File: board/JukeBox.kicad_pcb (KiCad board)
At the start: 2 copper layers, 78.5 x 80 mm, 56 parts, among them J1 USB_C_Receptacle_USB2.0, J2 Conn_01x02, J3 Conn_01x04, J4 Conn_01x03, SW1 SW_SPST, SW10 SW_SPST, SW11 SW_SPST, SW12 SW_SPST, SW2 SW_SPST, SW3 SW_SPST, SW4 SW_SPST, SW5 SW_SPST, SW6 SW_SPST, SW7 SW_SPST, SW8 SW_SPST, SW9 SW_SPST, U1 ATmega8U2-A, Y1 16MHz

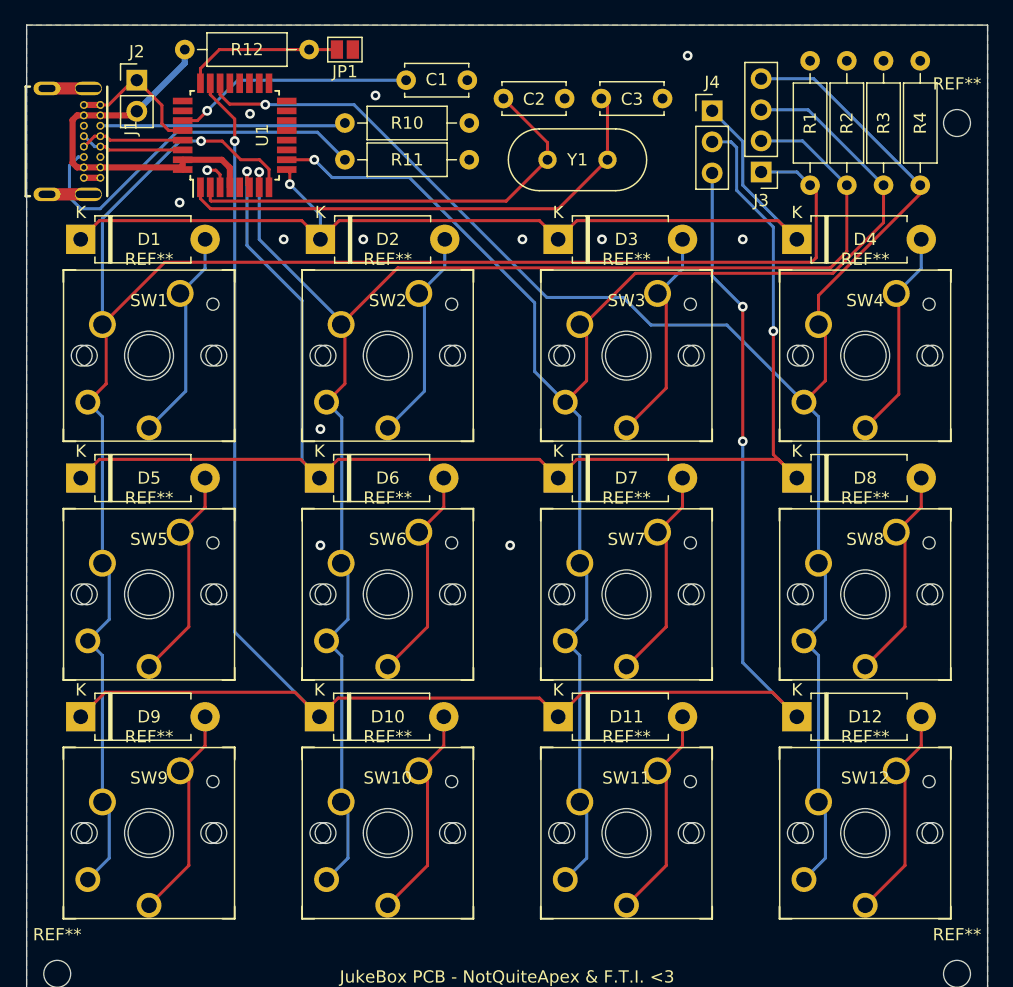
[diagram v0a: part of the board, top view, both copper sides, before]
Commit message: reroute everything again to move the mcu over
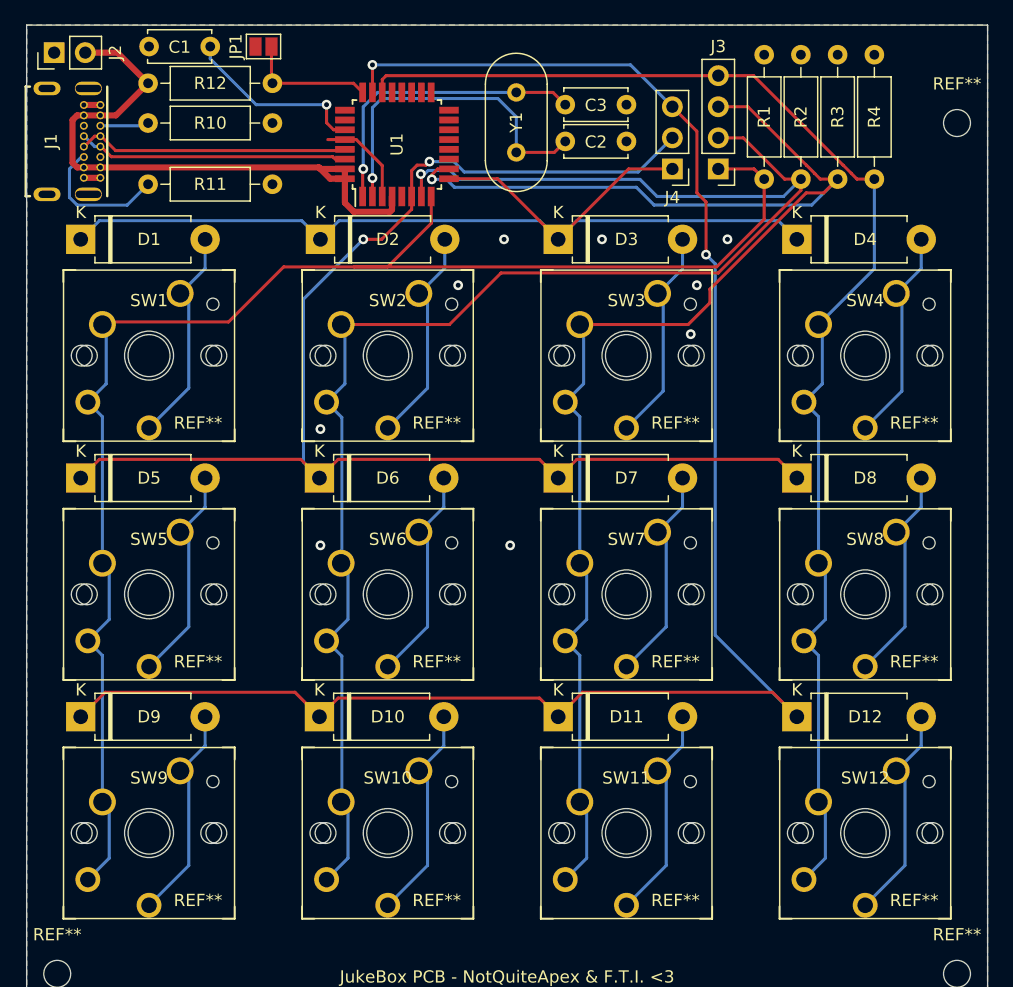
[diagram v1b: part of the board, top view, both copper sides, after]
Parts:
- moved C1 26.1 mm to (117.0, 36.8), turned to 0 degrees
- moved R11 16.2 mm to (116.9, 48.0)
- moved R10 16.1 mm to (116.9, 43.0)
- moved U1 13.3 mm to (137.2, 44.8)
- moved Y1 9.26 mm to (147.0, 40.5), turned to -90 degrees
- moved J2 7.12 mm to (109.2, 37.2), turned to 90 degrees
- moved JP1 6.65 mm to (126.3, 36.8), turned to 0 degrees
- moved C2 6.14 mm to (156.0, 44.5)
- moved J4 5.76 mm to (159.8, 46.8), turned to 180 degrees
- moved R12 4.07 mm to (127.1, 39.8)
- moved R1 3.78 mm to (167.2, 37.4)
- moved R2 3.78 mm to (170.2, 37.4)
- moved R3 3.78 mm to (173.2, 37.4)
- moved R4 3.78 mm to (176.2, 37.4)
- moved J3 3.51 mm to (163.5, 46.8)
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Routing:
- net COL_4: track 139.7 -> 107.6 mm, vias 1 -> 0
- net COL_1: track 147.2 -> 124.0 mm, vias 1 -> 0
- net ROW_3: track 165.8 -> 145.3 mm, vias 3 -> 2
- net Net-(J1-PadB5): track 30.5 -> 11.3 mm
- net +5V: track 31.5 -> 50.1 mm
- net Net-(C3-Pad2): track 41.4 -> 24.7 mm, vias 0 -> 1
- net Net-(J1-PadA5): track 20.1 -> 3.99 mm
- net /D+: track 8.56 -> 22.2 mm
- net /D-: track 8.54 -> 21.4 mm
- net COL_2: track 123.1 -> 134.7 mm
- net GND: track 22.0 -> 10.6 mm, vias 13 -> 9
- net Net-(C2-Pad2): track 36.5 -> 27.2 mm, vias 0 -> 1
- net ROW_2: track 122.4 -> 115.6 mm
- net Net-(C1-Pad2): track 19.6 -> 15.3 mm
- net ROW_1: track 82.5 -> 85.0 mm, vias 1 -> 0
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
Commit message: update models
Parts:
- renumbered REF** to _
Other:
- outline, holes or cut-outs redrawn
- board text added: "JukeBox - NotQuiteApex & F.T.I. <3"
- board text added: "https://jukebox.friendteam.biz"
- board text removed: "JukeBox PCB - NotQuiteApex & F.T.I. <3"

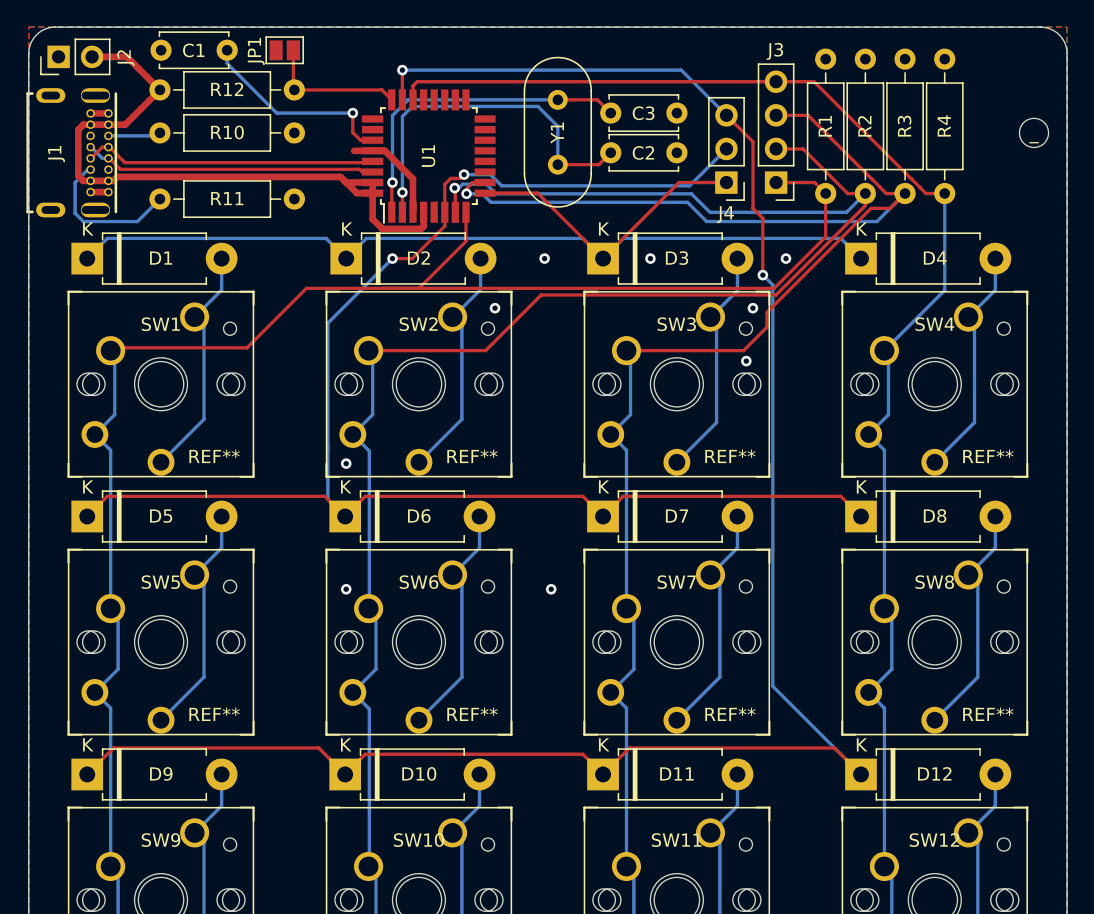
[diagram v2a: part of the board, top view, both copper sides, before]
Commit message: add footprint for screen addon, change all tht components to smt
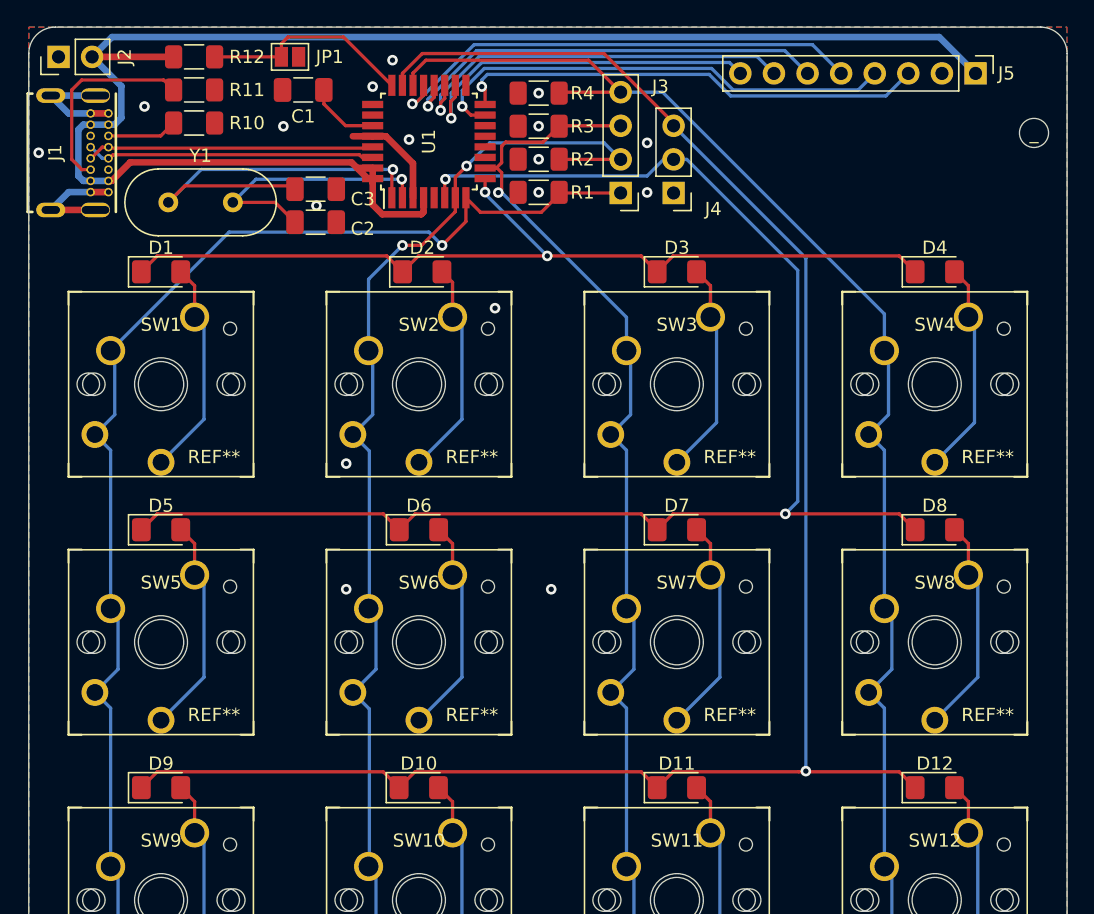
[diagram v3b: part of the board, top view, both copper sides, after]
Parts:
- added J5: Conn_01x08, Connector_PinHeader_2.54mm:PinHeader_1x08_P2.54mm_Vertical, F.Cu at (178.6, 38.5)
- C1, C2, C3: footprint Capacitor_THT:C_Disc_D5.0mm_W2.5mm_P5.00mm -> Capacitor_SMD:C_1206_3216Metric_Pad1.33x1.80mm_HandSolder
- D1, D10, D11, D12, D2, D3, D4, D5, D6, D7, D8, D9: footprint Diode_THT:D_DO-15_P10.16mm_Horizontal -> Diode_SMD:D_1206_3216Metric_Pad1.42x1.75mm_HandSolder
- R1, R10, R11, R12, R2, R3, R4: footprint Resistor_THT:R_Axial_DIN0207_L6.3mm_D2.5mm_P10.16mm_Horizontal -> Resistor_SMD:R_1206_3216Metric_Pad1.30x1.75mm_HandSolder
- Y1: footprint Crystal:Crystal_HC18-U_Vertical -> Crystal:Crystal_HC49-4H_Vertical
- moved R4 30.8 mm to (145.6, 40.0), turned to 0 degrees
- moved Y1 30.5 mm to (117.5, 48.2), turned to 0 degrees
- moved R3 28.2 mm to (145.6, 42.5), turned to 0 degrees
- moved C3 27.9 mm to (128.7, 47.2)
- moved C2 27.8 mm to (128.7, 49.8)
- moved R2 25.8 mm to (145.6, 45.0), turned to 0 degrees
- moved R1 23.9 mm to (145.6, 47.5), turned to 0 degrees
- moved J3 11.8 mm to (151.8, 47.5)
- moved C1 11.2 mm to (127.8, 39.8)
- moved R11 8.64 mm to (119.5, 39.8)
- moved R12 7.98 mm to (119.5, 37.2)
- moved D2 5.84 mm to (136.8, 53.5)
- moved D11 5.67 mm to (156.0, 92.5)
- moved D12 5.67 mm to (175.5, 92.5)
- moved D3 5.67 mm to (156.0, 53.5)
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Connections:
- U1 pad 15: unconnected-(U1-Pad15) -> CLK
- U1 pad 16: unconnected-(U1-Pad16) -> DIN
- U1 pad 18: unconnected-(U1-Pad18) -> BL
- U1 pad 19: unconnected-(U1-Pad19) -> RST
- U1 pad 20: unconnected-(U1-Pad20) -> DC
- U1 pad 21: unconnected-(U1-Pad21) -> CS
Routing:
- net +5V: track 50.4 -> 120.1 mm
- net COL_2: track 134.7 -> 84.4 mm, vias 1 -> 2
- net COL_3: track 124.7 -> 80.4 mm
- net CS: track 0.00 -> 37.0 mm, vias 0 -> 1
- net CLK: track 0.00 -> 36.3 mm, vias 0 -> 1
- net DIN: track 0.00 -> 35.8 mm, vias 0 -> 1
- net DC: track 0.00 -> 33.2 mm, vias 0 -> 1
- net RST: track 0.00 -> 30.1 mm, vias 0 -> 1
- net COL_1: track 124.0 -> 95.4 mm, vias 0 -> 1
- net BL: track 0.00 -> 27.7 mm, vias 0 -> 1
- net ROW_1: track 85.0 -> 69.3 mm, vias 0 -> 2
- net GND: track 10.6 -> 24.6 mm, vias 9 -> 17
- net Net-(C1-Pad2): track 15.3 -> 5.43 mm, vias 1 -> 0
- net Net-(C2-Pad2): track 27.2 -> 20.2 mm
- net ROW_3: track 145.3 -> 138.8 mm, vias 2 -> 1
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
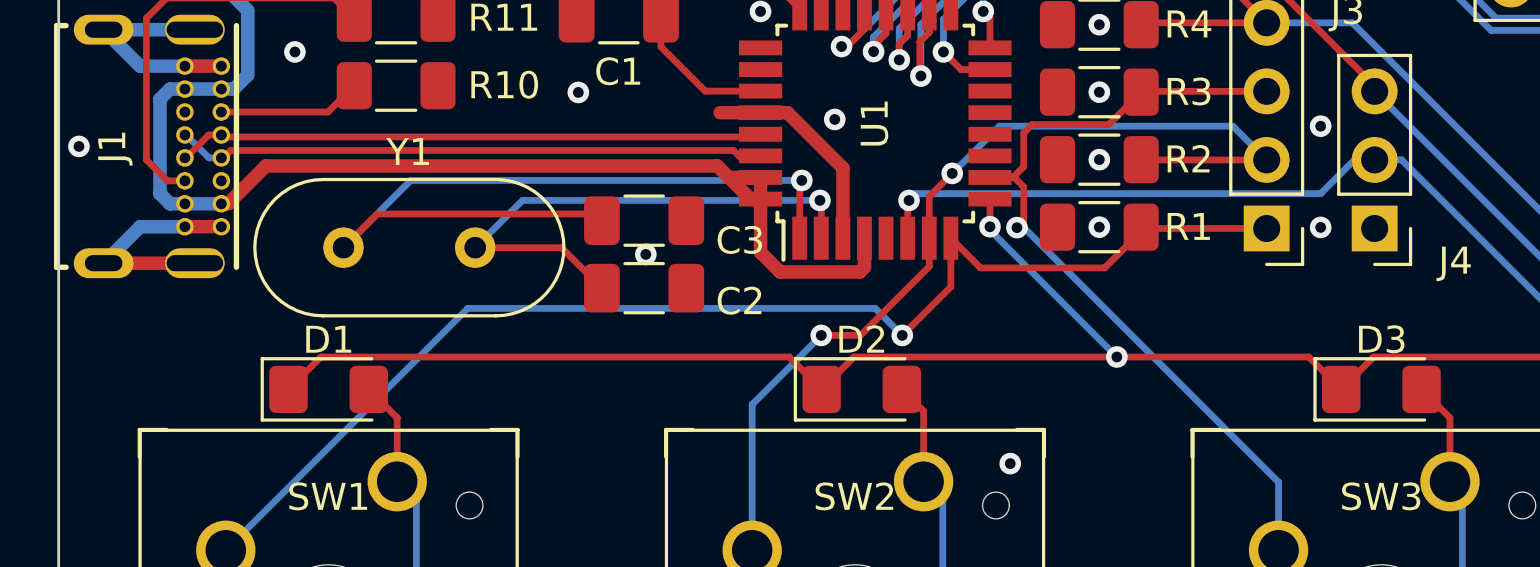
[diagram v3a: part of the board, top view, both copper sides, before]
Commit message: ran a drc, fix some errors
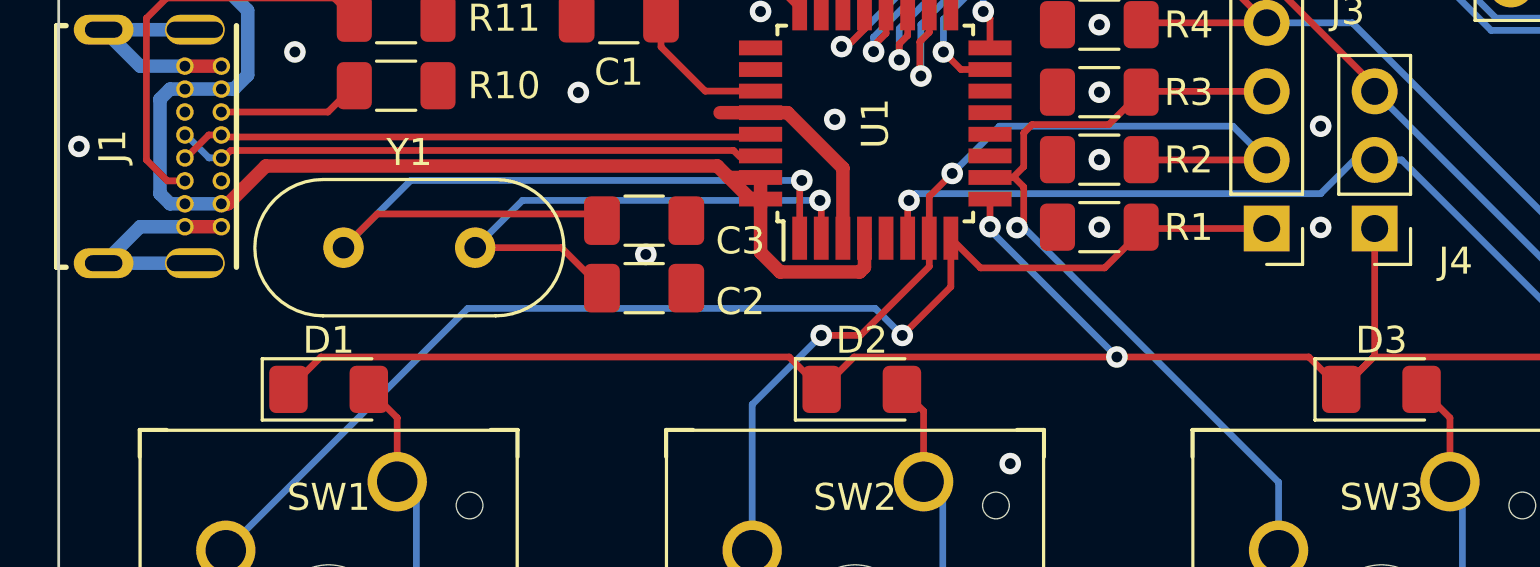
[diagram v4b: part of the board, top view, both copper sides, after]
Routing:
- net ROW_1: track 69.3 -> 75.8 mm
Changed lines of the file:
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@@
   (segment (start 136.05 45.3) (end 136.05 47.9) (width 0.5) (layer "F.Cu") (net 1))
   (segment (start 133 43.25) (end 131.5 43.25) (width 0.5) (layer "F.Cu") (net 1))
-  (segment (start 108.665 48.825) (end 112.045 48.825) (width 0.5) (layer "F.Cu") (net 1))
   (segment (start 111.675 41.525) (end 113.025 41.525) (width 0.5) (layer "F.Cu") (net 1))
   (segment (start 133 43.25) (end 134 43.25) (width 0.5) (layer "F.Cu") (net 1))
@@
   (segment (start 110.015 47.475) (end 108.665 48.825) (width 0.5) (layer "B.Cu") (net 1))
   (segment (start 111.675 47.475) (end 110.015 47.475) (width 0.5) (layer "B.Cu") (net 1))
+  (segment (start 108.665 48.825) (end 112.045 48.825) (width 0.5) (layer "B.Cu") (net 1))
   (segment (start 112.045 40.175) (end 108.665 40.175) (width 0.5) (layer "B.Cu") (net 1))
   (segment (start 111.675 41.525) (end 110.015 41.525) (width 0.5) (layer "B.Cu") (net 1))
@@
   (segment (start 134.528649 45.759985) (end 120.040015 45.759985) (width 0.25) (layer "B.Cu") (net 4))
   (segment (start 153.3125 52.3) (end 154.5125 53.5) (width 0.25) (layer "F.Cu") (net 5))
+  (segment (start 155.75 47.54) (end 155.75 52.2625) (width 0.25) (layer "F.Cu") (net 5))
   (segment (start 136.4625 52.3) (end 146.2 52.3) (width 0.25) (layer "F.Cu") (net 5))
   (segment (start 155.7125 52.3) (end 154.5125 53.5) (width 0.25) (layer "F.Cu") (net 5))
@@
   (segment (start 141.5 46.45) (end 141.5 47.4755) (width 0.25) (layer "F.Cu") (net 5))
   (segment (start 134.0625 52.3) (end 135.2625 53.5) (width 0.25) (layer "F.Cu") (net 5))
+  (segment (start 155.75 52.2625) (end 154.5125 53.5) (width 0.25) (layer "F.Cu") (net 5))
   (segment (start 115.5125 53.5) (end 116.7125 52.3) (width 0.25) (layer "F.Cu") (net 5))
   (segment (start 155.7125 52.3) (end 172.8125 52.3) (width 0.25) (layer "F.Cu") (net 5))
@@
   (segment (start 142.75 45.25) (end 142.75 44) (width 0.25) (layer "F.Cu") (net 30))
   (segment (start 151.75 42.46) (end 147.13 42.46) (width 0.25) (layer "F.Cu") (net 30))
-  (segment (start 142.75 46) (end 142.75 47.257102) (width 0.25) (layer "F.Cu") (net 30))
+  (segment (start 142.75 46) (end 142.4 45.65) (width 0.25) (layer "F.Cu") (net 30))
   (segment (start 142.75 44) (end 143.06 43.69) (width 0.25) (layer "F.Cu") (net 30))
   (segment (start 141.5 45.65) (end 142.35 45.65) (width 0.25) (layer "F.Cu") (net 30))
-  (segment (start 141.5 45.65) (end 142.4 45.65) (width 0.25) (layer "F.Cu") (net 30))
+  (segment (start 142.75 47.257102) (end 142.75 46) (width 0.25) (layer "F.Cu") (net 30))
   (segment (start 147.13 42.46) (end 147.1 42.49) (width 0.25) (layer "F.Cu") (net 30))
   (segment (start 145.9 43.69) (end 147.1 42.49) (width 0.25) (layer "F.Cu") (net 30))
   (segment (start 143.06 43.69) (end 145.9 43.69) (width 0.25) (layer "F.Cu") (net 30))
-  (segment (start 142.4 45.65) (end 142.75 46) (width 0.25) (layer "F.Cu") (net 30))
-  (segment (start 142.75 47.257102) (end 142.498969 47.508133) (width 0.25) (layer "F.Cu") (net 30))
+  (segment (start 142.498969 47.508133) (end 142.75 47.257102) (width 0.25) (layer "F.Cu") (net 30))
+  (segment (start 142.4 45.65) (end 141.5 45.65) (width 0.25) (layer "F.Cu") (net 30))
   (via (at 142.498969 47.508133) (size 0.8) (drill 0.4) (layers "F.Cu" "B.Cu") (net 30))
   (segment (start 152.5 64.3) (end 152.5 59.77) (width 0.25) (layer "B.Cu") (net 30))
   (segment (start 152.75 79.52) (end 152.19 78.96) (width 0.25) (layer "B.Cu") (net 30))
   (segment (start 152.19 56.94) (end 152.19 59.46) (width 0.25) (layer "B.Cu") (net 30))
+  (segment (start 142.758133 47.508133) (end 152.19 56.94) (width 0.25) (layer "B.Cu") (net 30))
   (segment (start 152.75 103.05) (end 152.75 99.02) (width 0.25) (layer "B.Cu") (net 30))
   (segment (start 152.5 59.77) (end 152.19 59.46) (width 0.25) (layer "B.Cu") (net 30))
@@
   (segment (start 151 65.8) (end 152.19 66.99) (width 0.25) (layer "B.Cu") (net 30))
   (segment (start 151 65.8) (end 152.5 64.3) (width 0.25) (layer "B.Cu") (net 30))
+  (segment (start 142.498969 47.508133) (end 142.758133 47.508133) (width 0.25) (layer "B.Cu") (net 30))
   (segment (start 152.75 99.02) (end 152.19 98.46) (width 0.25) (layer "B.Cu") (net 30))
   (segment (start 151 85.3) (end 152.19 86.49) (width 0.25) (layer "B.Cu") (net 30))
-  (segment (start 142.498969 47.508133) (end 142.758133 47.508133) (width 0.25) (layer "B.Cu") (net 30))
   (segment (start 151 85.3) (end 152.75 83.55) (width 0.25) (layer "B.Cu") (net 30))
   (segment (start 152.75 83.55) (end 152.75 79.52) (width 0.25) (layer "B.Cu") (net 30))
   (segment (start 152.19 66.99) (end 152.19 78.96) (width 0.25) (layer "B.Cu") (net 30))
-  (segment (start 142.758133 47.508133) (end 152.19 56.94) (width 0.25) (layer "B.Cu") (net 30))
   (segment (start 152.19 86.49) (end 152.19 98.46) (width 0.25) (layer "B.Cu") (net 30))
   (segment (start 136.05 39.4) (end 136.05 38.475) (width 0.25) (layer "F.Cu") (net 31))
